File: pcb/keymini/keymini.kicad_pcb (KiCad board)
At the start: 2 copper layers, 205.4 x 88.6 mm, 85 parts, among them J1 USB_C_Receptacle_USB2.0_16P, SW1A SW_Push, SW1B SW_Push, SW1C SW_Push, SW1D SW_Push, SW1E SW_Push, SW1F SW_Push, SW1G SW_Push, SW1H SW_Push, SW1I SW_Push, SW1J SW_Push, SW2A SW_Push, SW2B SW_Push, SW2C SW_Push, SW2D SW_Push, SW2E SW_Push, SW2F SW_Push, SW2G SW_Push, SW2H SW_Push, SW2I SW_Push, SW2J SW_Push, SW3A SW_Push, SW3B SW_Push, SW3C SW_Push, SW3D SW_Push, SW3E SW_Push, SW3F SW_Push, SW3G SW_Push, SW3H SW_Push, SW3I SW_Push, SW3J SW_Push, SW4C SW_Push, SW4D SW_Push, SW4E SW_Push, SW4F SW_Push, SW4G SW_Push, SW4H SW_Push, U1 STM32F072CBT6, U2 XC6206P332MR

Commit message: trace tweeks
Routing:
- net ROW3: track 233.7 -> 232.0 mm

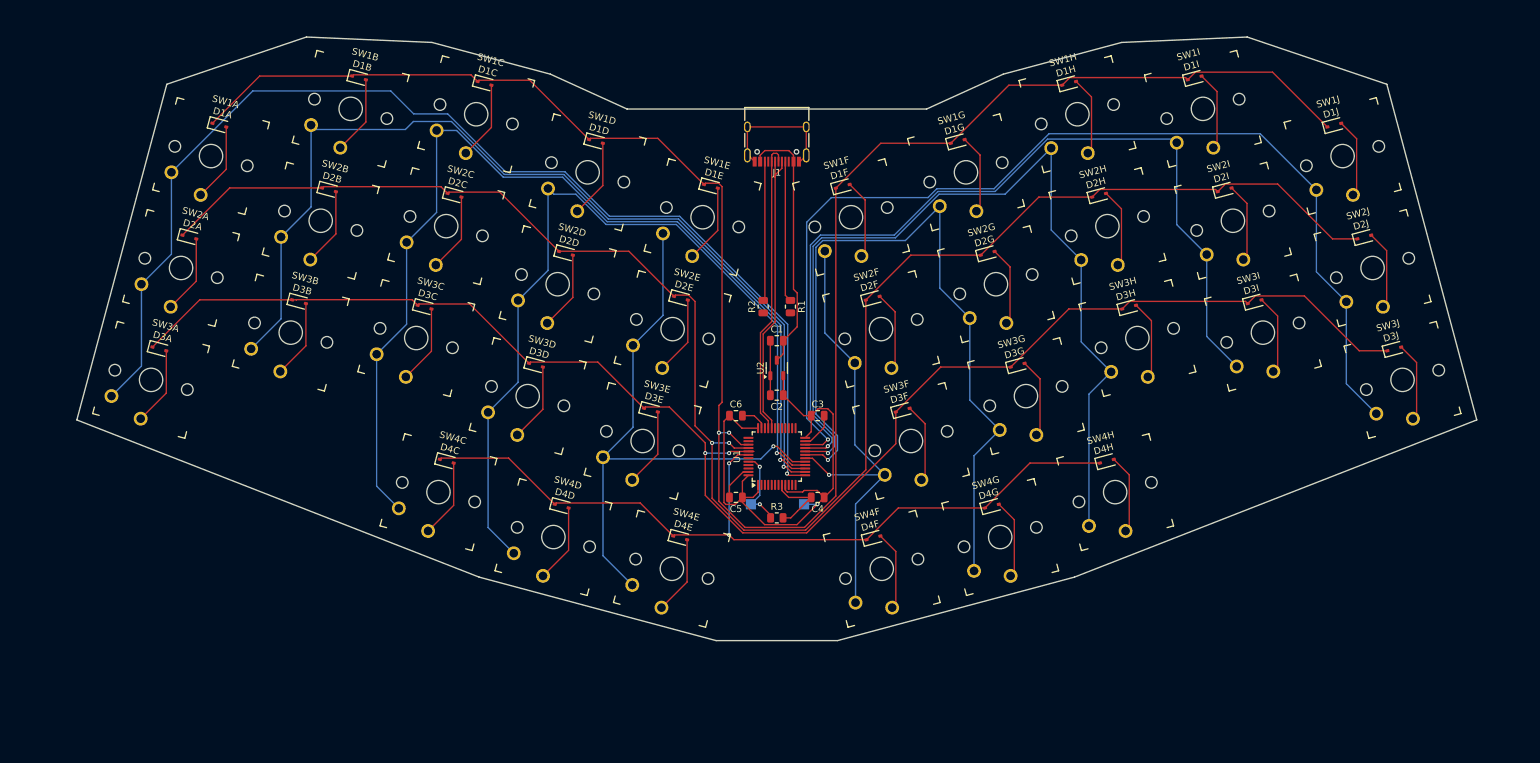
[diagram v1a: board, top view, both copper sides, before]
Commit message: Add SWD connector
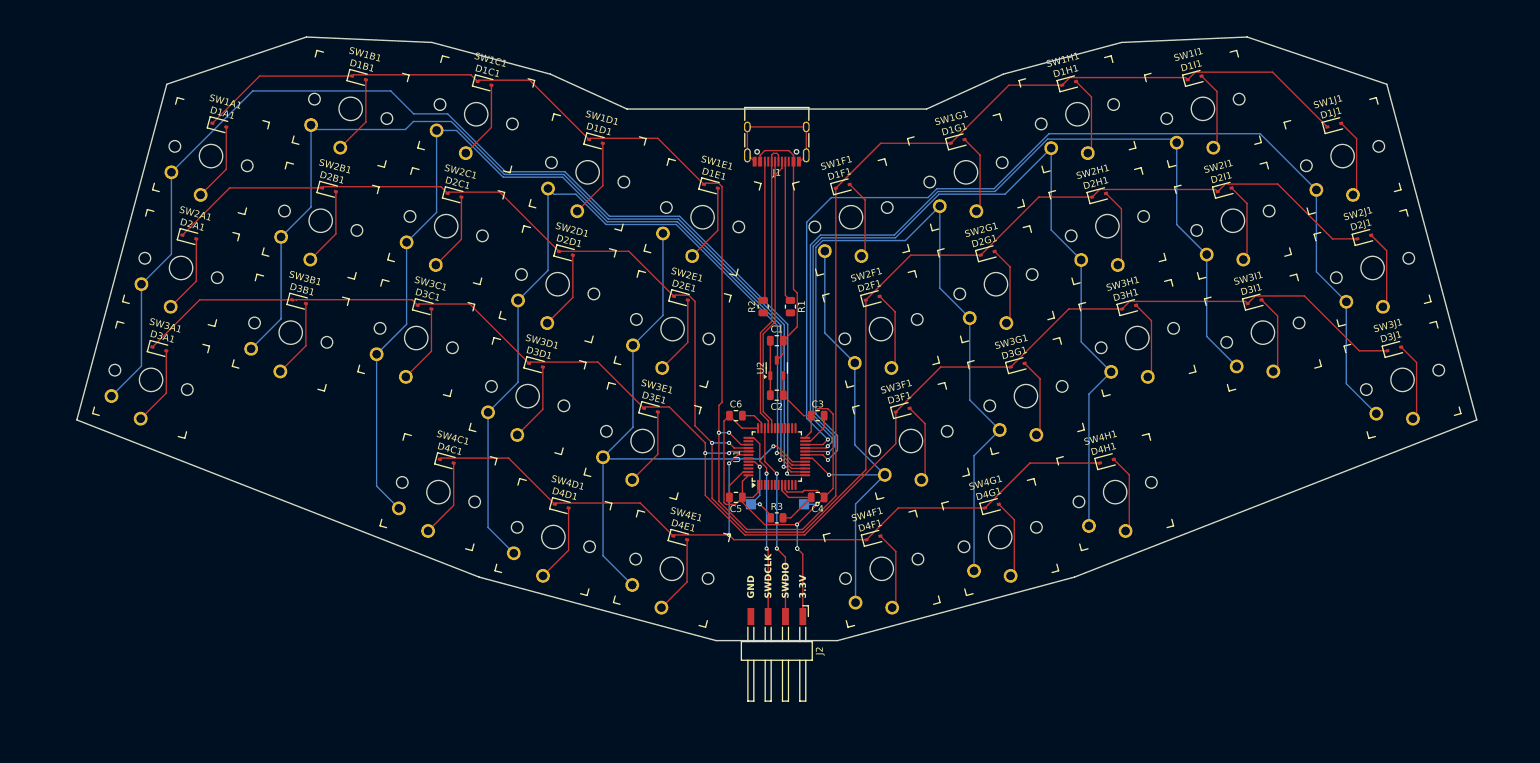
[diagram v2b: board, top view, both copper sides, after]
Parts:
- added J2: Conn_01x04, Connector_Harwin:Harwin_M20-89004xx_1x04_P2.54mm_Horizontal, F.Cu at (150.0, 110.0)
- renumbered BOOT to BOOT1, D1A to D1A1, D1B to D1B1, D1C to D1C1, D1D to D1D1, D1E to D1E1, D1F to D1F1, D1G to D1G1, D1H to D1H1, D1I to D1I1, D1J to D1J1, D2A to D2A1, D2B to D2B1, D2C to D2C1, D2D to D2D1, D2E to D2E1, D2F to D2F1, D2G to D2G1, D2H to D2H1, D2I to D2I1, D2J to D2J1, D3A to D3A1, D3B to D3B1, D3C to D3C1, D3D to D3D1, D3E to D3E1, D3F to D3F1, D3G to D3G1, D3H to D3H1, D3I to D3I1, D3J to D3J1, D4C to D4C1, D4D to D4D1, D4E to D4E1, D4F to D4F1, D4G to D4G1, D4H to D4H1, SW1A to SW1A1, SW1B to SW1B1, SW1C to SW1C1, SW1D to SW1D1, SW1E to SW1E1, SW1F to SW1F1, SW1G to SW1G1, SW1H to SW1H1, SW1I to SW1I1, SW1J to SW1J1, SW2A to SW2A1, SW2B to SW2B1, SW2C to SW2C1, SW2D to SW2D1, SW2E to SW2E1, SW2F to SW2F1, SW2G to SW2G1, SW2H to SW2H1, SW2I to SW2I1, SW2J to SW2J1, SW3A to SW3A1, SW3B to SW3B1, SW3C to SW3C1, SW3D to SW3D1, SW3E to SW3E1, SW3F to SW3F1, SW3G to SW3G1, SW3H to SW3H1, SW3I to SW3I1, SW3J to SW3J1, SW4C to SW4C1, SW4D to SW4D1, SW4E to SW4E1, SW4F to SW4F1, SW4G to SW4G1, SW4H to SW4H1
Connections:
- U1 pad 37: SWCLK -> SWDCLK
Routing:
- net SWDIO: track 0.00 -> 28.9 mm, vias 0 -> 2
- net SWDCLK: track 0.00 -> 27.9 mm, vias 0 -> 2
- net +3.3V: track 82.0 -> 95.8 mm, vias 1 -> 4
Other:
- board text added: "3.3V"
- board text added: "GND"
- board text added: "SWDCLK"
- board text added: "SWDIO"

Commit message: complete rooting with swo and ground plate
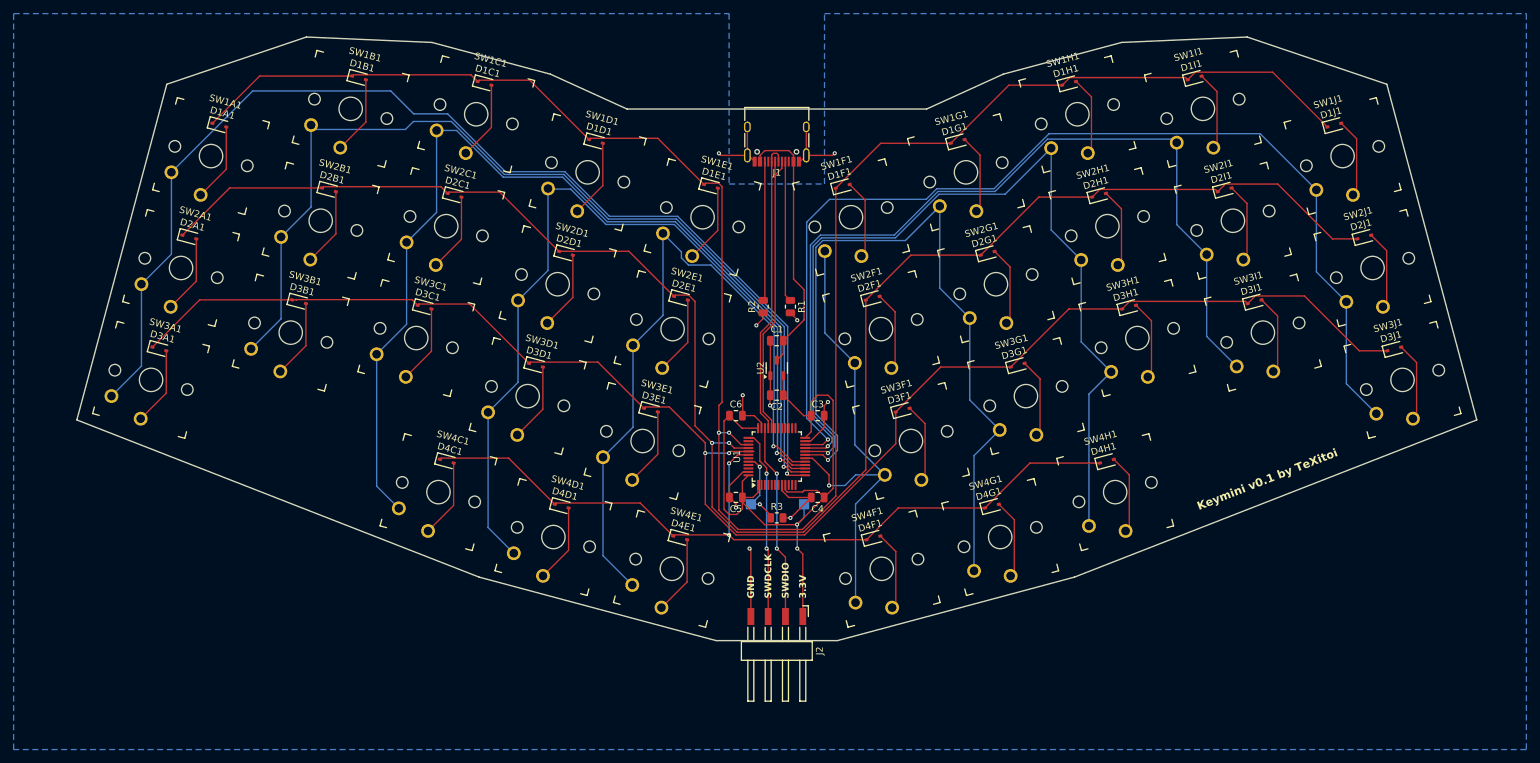
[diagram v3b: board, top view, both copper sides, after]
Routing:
- net GND: track 53.6 -> 76.0 mm, vias 0 -> 10
- net COLE: track 88.5 -> 102.9 mm
- net +3.3V: track 95.8 -> 104.1 mm, vias 4 -> 2
- net COLF: track 69.7 -> 71.9 mm
- net +5V: track 37.9 -> 38.8 mm
- net ROW3: track 232.2 -> 233.0 mm
- net ROW1: track 285.3 -> 286.1 mm
- net ROW2: track 257.2 -> 257.9 mm
- added copper zone on B.Cu, net GND
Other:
- board text added: "Keymini v0.1 by TeXitoi"

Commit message: Tweeks
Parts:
- renumbered BOOT1 to BOOT
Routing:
- net GND: track 76.0 -> 152.3 mm, vias 10 -> 8

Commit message: make PCB checker happy
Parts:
- renumbered BOOT to BOOT1
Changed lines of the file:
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@@
 		(descr "https://www.mouser.com/ds/2/60/RS-282G05A-SM_RT-1159762.pdf")
 		(tags "SPST button tactile switch")
-		(property "Reference" "BOOT"
+		(property "Reference" "BOOT1"
 			(at 0 2.6 0)
 			(layer "B.SilkS")
